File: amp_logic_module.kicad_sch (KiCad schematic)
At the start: 41 parts, among them J23 Screw_Terminal_01x02, J27 Screw_Terminal_01x02, U10 PCM5102A, U16 TPA3116D2DADR

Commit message: Fixed most ERC checks
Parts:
- renumbered C39 to C16, C40 to C17, C41 to C18, C42 to C19, C23 to C20, C43 to C21, C44 to C22, C24 to C23, C25 to C24, C45 to C25, C48 to C26, C47 to C27, C46 to C28, C28 to C29, C26 to C30, C27 to C31, C29 to C32, C37 to C33, C38 to C34, C36 to C35, C33 to C36, C35 to C37, C31 to C38, C30 to C39, C34 to C40, C32 to C41, J23 to J8, J27 to J9, R16 to R11, R15 to R12, R17 to R13, R18 to R14, R19 to R15, R20 to R16, R21 to R17, U16 to U11
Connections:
- no-connect marks 0 -> 5

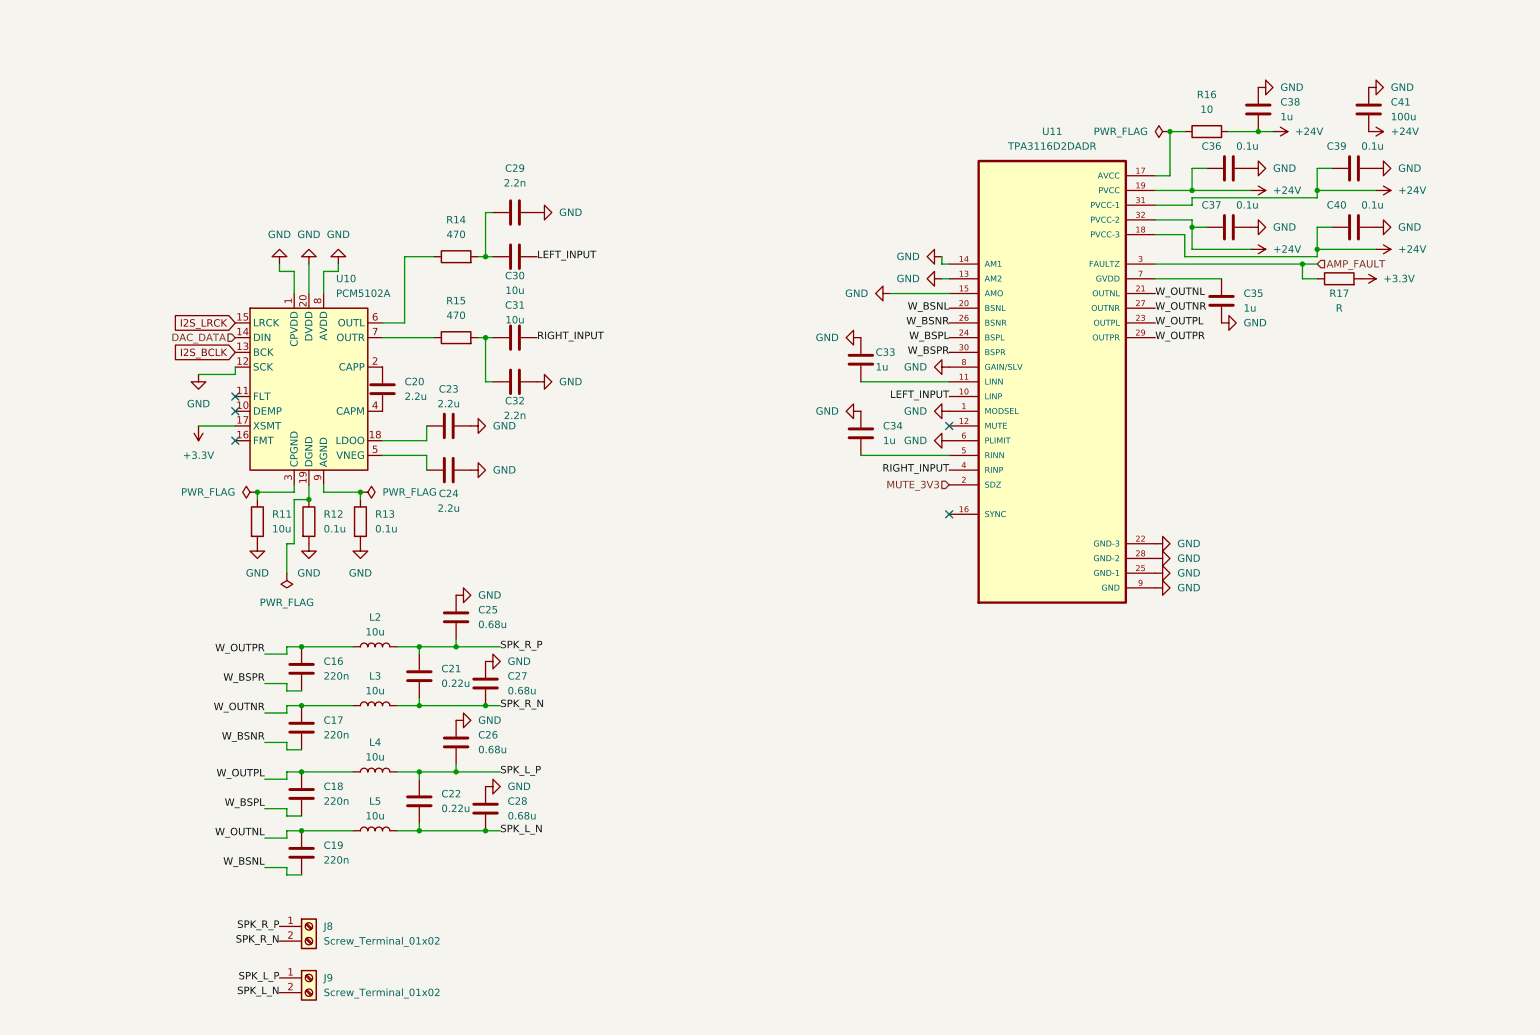
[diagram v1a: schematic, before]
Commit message: Footprinting done (warnings on schematic side but pcb import works fine)
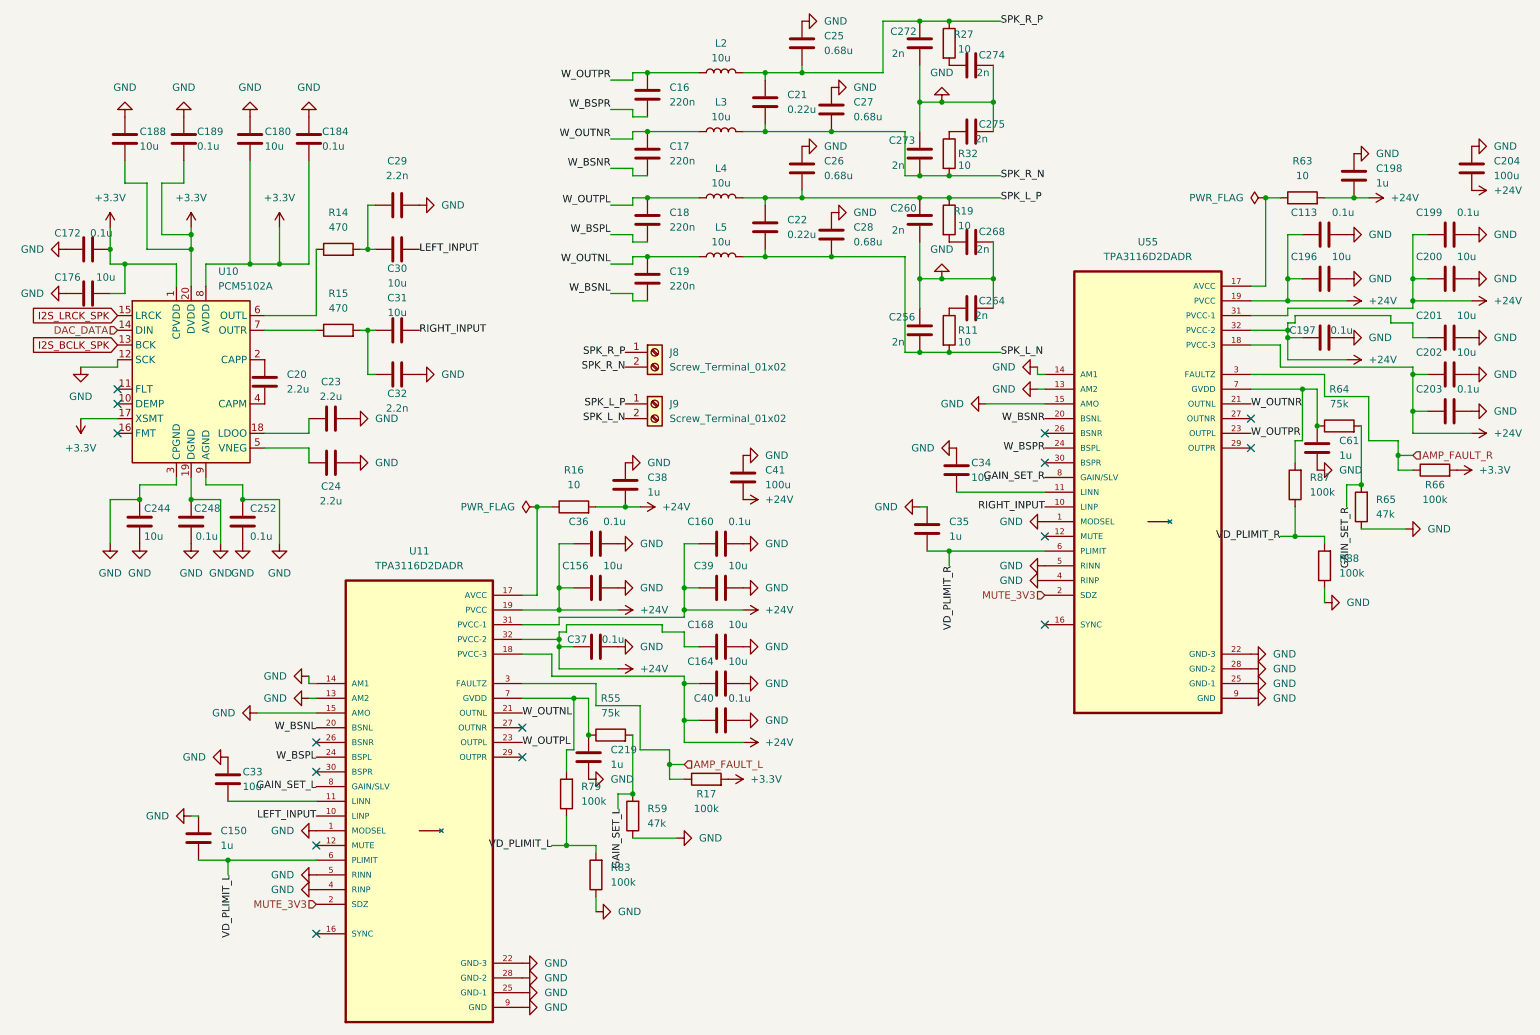
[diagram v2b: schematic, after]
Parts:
- removed R12, R13: 0.1u, symbol Device:R
- added C113, C160, C172, C184, C189, C197, C199, C203, C248, C252: 0.1u, Capacitor_SMD:C_0603_1608Metric, symbol Device:C
- added C150, C198, C219, C61: 1u, Capacitor_SMD:C_0603_1608Metric, symbol Device:C
- added C156, C164, C168, C176, C180, C188, C196, C200, C201, C202, C244: 10u, Capacitor_SMD:C_0603_1608Metric, symbol Device:C
- added C204: 100u, Capacitor_SMD:C_0603_1608Metric, symbol Device:C
- added C256, C260, C264, C268, C272, C273, C274, C275: 2n, Capacitor_SMD:C_0805_2012Metric, symbol Device:C
- added R19, R27, R32, R63: 10, Resistor_SMD:R_0805_2012Metric, symbol Device:R
- added R55, R64: 75k, Resistor_SMD:R_0603_1608Metric, symbol Device:R
- added R59, R65: 47k, Resistor_SMD:R_0603_1608Metric, symbol Device:R
- added R66, R79, R83, R87, R88: 100k, Resistor_SMD:R_0603_1608Metric, symbol Device:R
- added U55: TPA3116D2DADR, TPA3116D2DADR:SOP65P810X115-33N, symbol TPA3116D2DADR:TPA3116D2DADR
- C16, C17, C18, C19, C20, C21, C22, C23, C24, C25, C26, C27, C28, C29, C30, C31, C32, C35, C36, C37, C38, C40, C41: footprint (none) -> Capacitor_SMD:C_0603_1608Metric
- C33, C34: value 1u -> 10u; footprint (none) -> Capacitor_SMD:C_0603_1608Metric
- C39: value 0.1u -> 10u; footprint (none) -> Capacitor_SMD:C_0603_1608Metric
- J8, J9: footprint (none) -> TerminalBlock_Phoenix:CONN-TH_2P-P5.00_WJ500V-5.08-2P; LCSC Part # (none) -> C8465
- L2: footprint (none) -> Inductor_SMD:IND-SMD_L10.4-W10.3; Current Saturation (none) -> 5.6A; LCSC (none) -> C9935
- L3, L4, L5: footprint (none) -> Inductor_SMD:IND-SMD_L10.4-W10.3
- R11: value 10u -> 10; footprint (none) -> Resistor_SMD:R_0805_2012Metric
- R14, R15: footprint (none) -> Resistor_SMD:R_0603_1608Metric
- R16: footprint (none) -> Resistor_SMD:R_0805_2012Metric
- R17: value R -> 100k; footprint (none) -> Resistor_SMD:R_0603_1608Metric
- U10: LCSC Part # (none) -> C107671
- U11: symbol TPA3116D2:TPA3116D2DADR -> TPA3116D2DADR:TPA3116D2DADR
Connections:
- net +24V: now also C113.2, C156.2, C160.2, C164.2, C168.2, C196.2, C197.2, C198.2, C199.2, C200.2, C201.2, C202.2, C203.2, C204.2, R63.2, U55.18 (PVCC-3), U55.19 (PVCC), U55.31 (PVCC-1), U55.32 (PVCC-2)
- net +3.3V: now also U10.1 (CPVDD), U10.20 (DVDD), U10.8 (AVDD), C172.2, C176.2, C180.2, C184.2, C188.2, C189.2, R66.2
- net GND: now also U10.19 (DGND), U10.3 (CPGND), U10.9 (AGND), U11.4 (RINP), U11.5 (RINN), C113.1, C150.2, C156.1, C160.1, C164.1, C168.1, C172.1, C176.1, C180.1, C184.1, C188.1, C189.1, C196.1, C197.1, C198.1, C199.1, C200.1, C201.1, C202.1, C203.1, C204.1, C219.2, C244.1, C244.2, C248.1, C248.2, C252.1, C252.2, C256.1, C260.2, C264.2, C268.2, C272.2, C273.1, C274.2, C275.2, C61.2, R59.1, R65.1, R83.1, R88.1, U55.1 (MODSEL), U55.13 (AM2), U55.14 (AM1), U55.15 (AMO), U55.22 (GND-3), U55.25 (GND-1), U55.28 (GND-2), U55.4 (RINP), U55.5 (RINN), U55.9 (GND); no longer R11.2, U10.1 (CPVDD), U10.20 (DVDD), U10.8 (AVDD), U11.6 (PLIMIT), U11.8 (GAIN/SLV)
- net MUTE_3V3: now also U55.2 (SDZ)
- net RIGHT_INPUT: now also U55.10 (LINP); no longer U11.4 (RINP)
- net SPK_L_N: now also R11.2, C256.2
- net SPK_L_P: now also C260.1, R19.1
- net SPK_R_N: now also C273.2, R32.2
- net SPK_R_P: now also C272.1, R27.1
- net W_BSNR: now also U55.20 (BSNL); no longer U11.26 (BSNR)
- net W_BSPR: now also U55.24 (BSPL); no longer U11.30 (BSPR)
- net W_OUTNR: now also U55.21 (OUTNL); no longer U11.27 (OUTNR)
- net W_OUTPR: now also U55.23 (OUTPL); no longer U11.29 (OUTPR)
- net at R11.1: now also C264.1; no longer U10.3 (CPGND)
- net at C34.2: now also U55.11 (LINN); no longer U11.5 (RINN)
- net at U11.7 (GVDD): now also C219.1, R55.1, R79.2; no longer C35.1
- net AMP_FAULT renamed AMP_FAULT_L
- net I2S_BCLK renamed I2S_BCLK_SPK
- net I2S_LRCK renamed I2S_LRCK_SPK
- new net: R63.1, U55.17 (AVCC)
- new net: C61.1, R64.1, R87.2, U55.7 (GVDD)
- new net: C268.1, R19.2
- new net: C274.1, R27.2
- new net: C275.1, R32.1
- new net AMP_FAULT_R: R66.1, U55.3 (FAULTZ)
- new net GAIN_SET_L: R55.2, R59.2, U11.8 (GAIN/SLV)
- new net GAIN_SET_R: R64.2, R65.2, U55.8 (GAIN/SLV)
- new net VD_PLIMIT_L: C150.1, R79.1, R83.2, U11.6 (PLIMIT)
- new net VD_PLIMIT_R: C35.1, R87.1, R88.2, U55.6 (PLIMIT)
- no-connect marks 5 -> 15
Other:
- moved on the sheet: C16, C17, C18, C19, C20, C21, C22, C23, C24, C25, C26, C27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

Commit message: Minor schematic changes
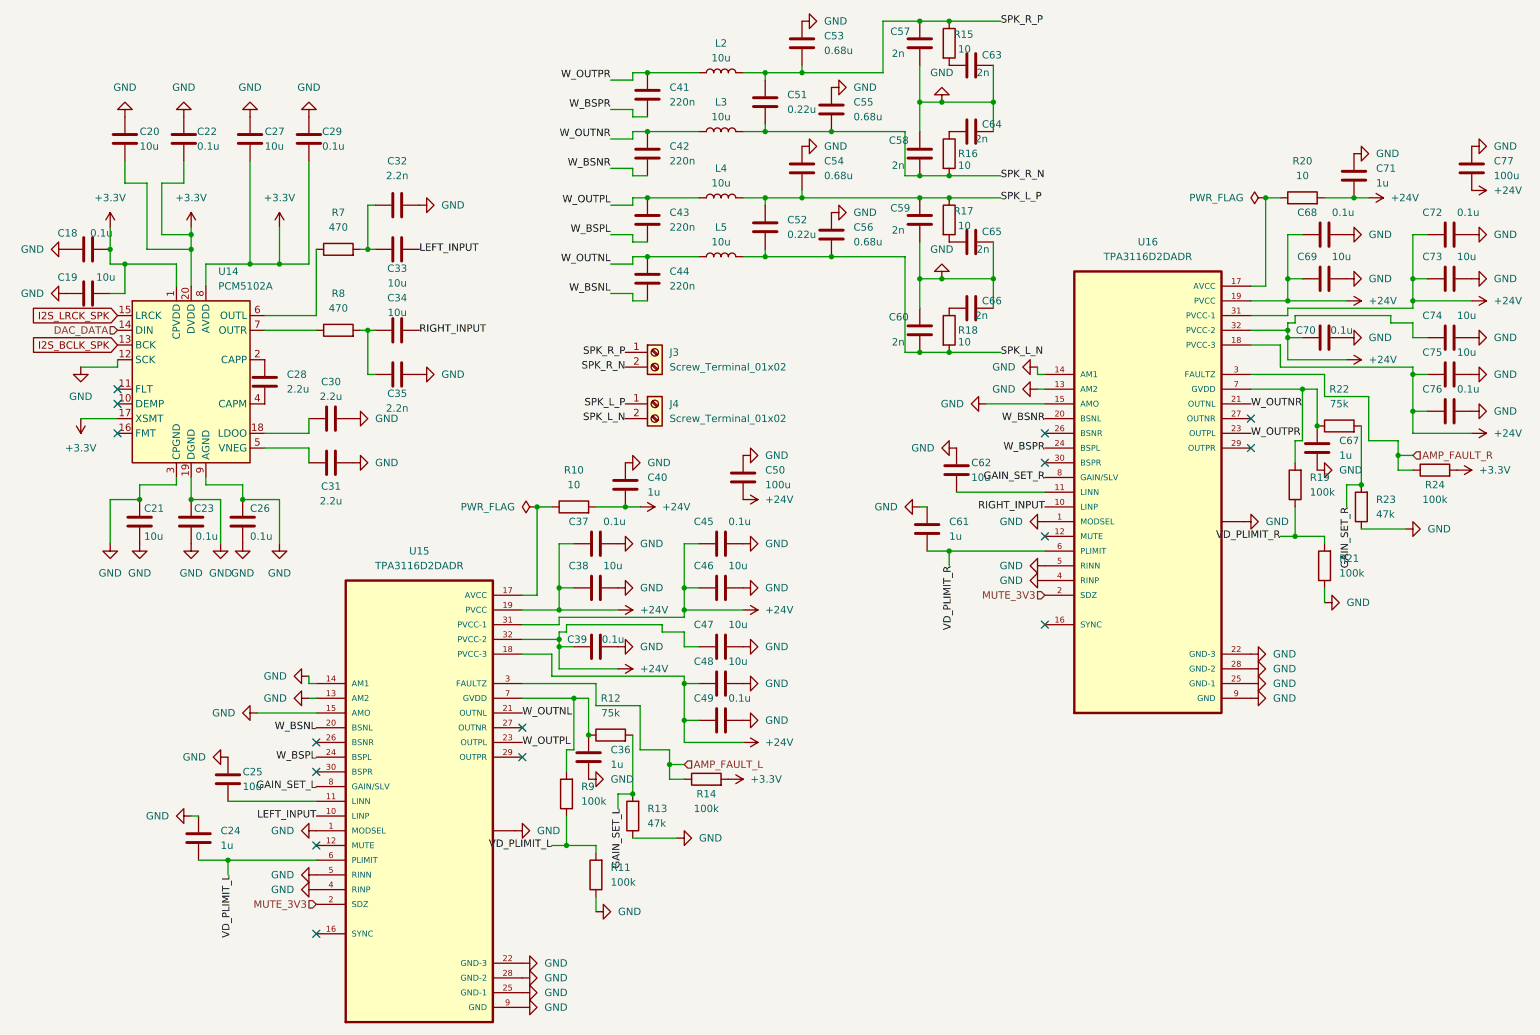
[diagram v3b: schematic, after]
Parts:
- R23: renamed from R65; LCSC Part # (none) -> C25819
- renumbered C172 to C18, C176 to C19, C188 to C20, C244 to C21, C189 to C22, C248 to C23, C150 to C24, C33 to C25, C252 to C26, C180 to C27, C20 to C28, C184 to C29, C23 to C30, C24 to C31, C29 to C32, C30 to C33, C31 to C34, C32 to C35, C219 to C36, C36 to C37, C156 to C38, C37 to C39, C38 to C40, C16 to C41, C17 to C42, C18 to C43, C19 to C44, C160 to C45, C39 to C46, C168 to C47, C164 to C48, C40 to C49, C41 to C50, C21 to C51, C22 to C52, C25 to C53, C26 to C54, C27 to C55, C28 to C56, C272 to C57, C273 to C58, C260 to C59, C256 to C60, C35 to C61, C34 to C62, C274 to C63, C275 to C64, C268 to C65, C264 to C66, C61 to C67, C113 to C68, C196 to C69, C197 to C70, C198 to C71, C199 to C72, C200 to C73, C201 to C74, C202 to C75, C203 to C76, C204 to C77, J8 to J3, J9 to J4, R16 to R10, R83 to R11, R55 to R12, R59 to R13, R17 to R14, R27 to R15, R32 to R16, R19 to R17, R11 to R18, R87 to R19, R63 to R20, R88 to R21, R64 to R22, R66 to R24, R14 to R7, R15 to R8, R79 to R9, U10 to U14, U11 to U15, U55 to U16
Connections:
- net GND: now also U15.33 (PAD), U16.33 (PAD)
